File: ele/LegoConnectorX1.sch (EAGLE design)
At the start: 2 parts, among them X1 NXT-SOCKET

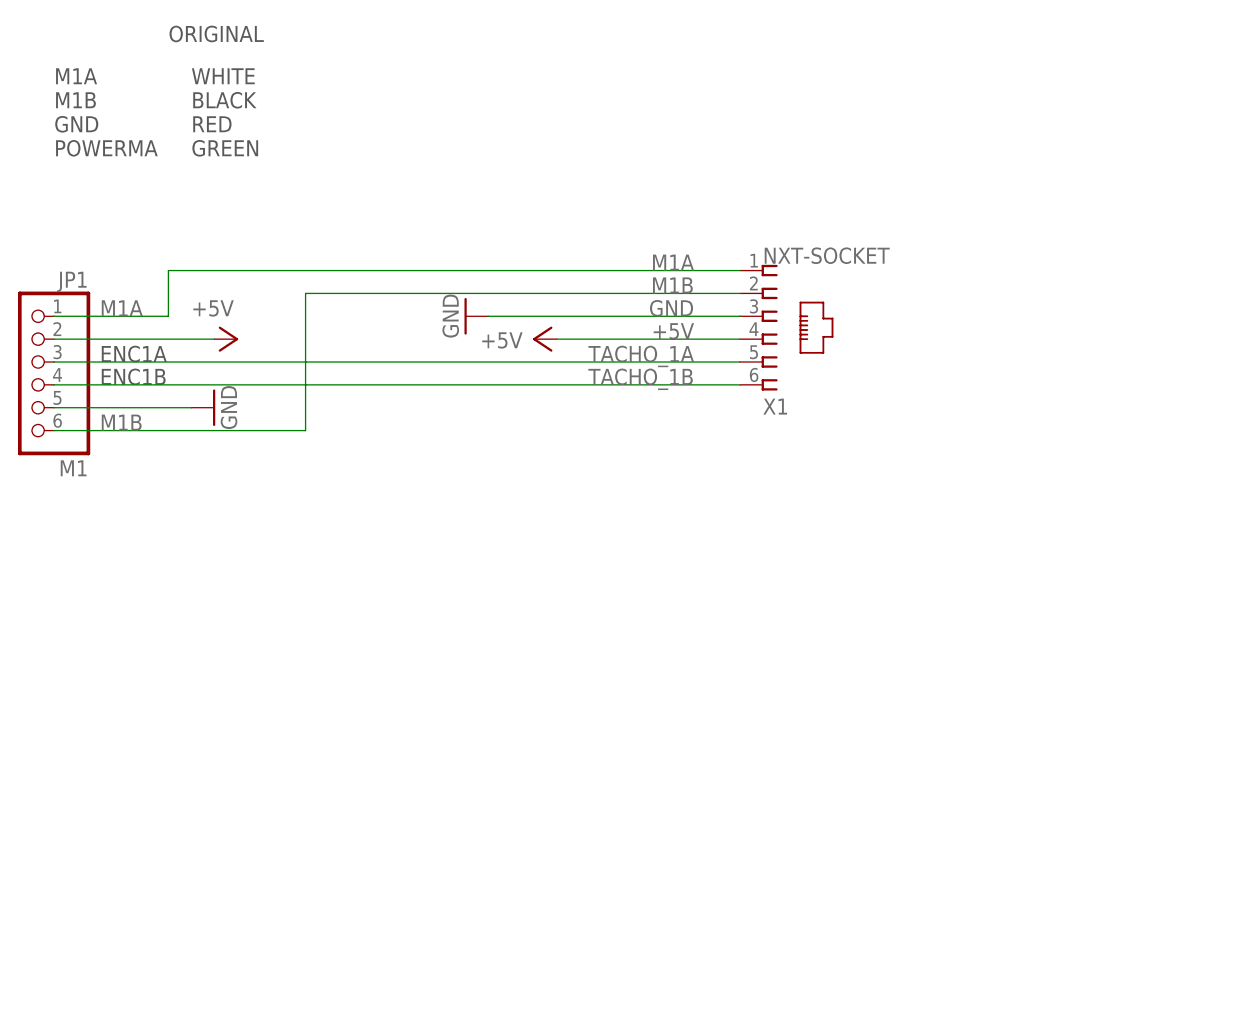
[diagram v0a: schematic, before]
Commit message: Add licenses to Eagle files
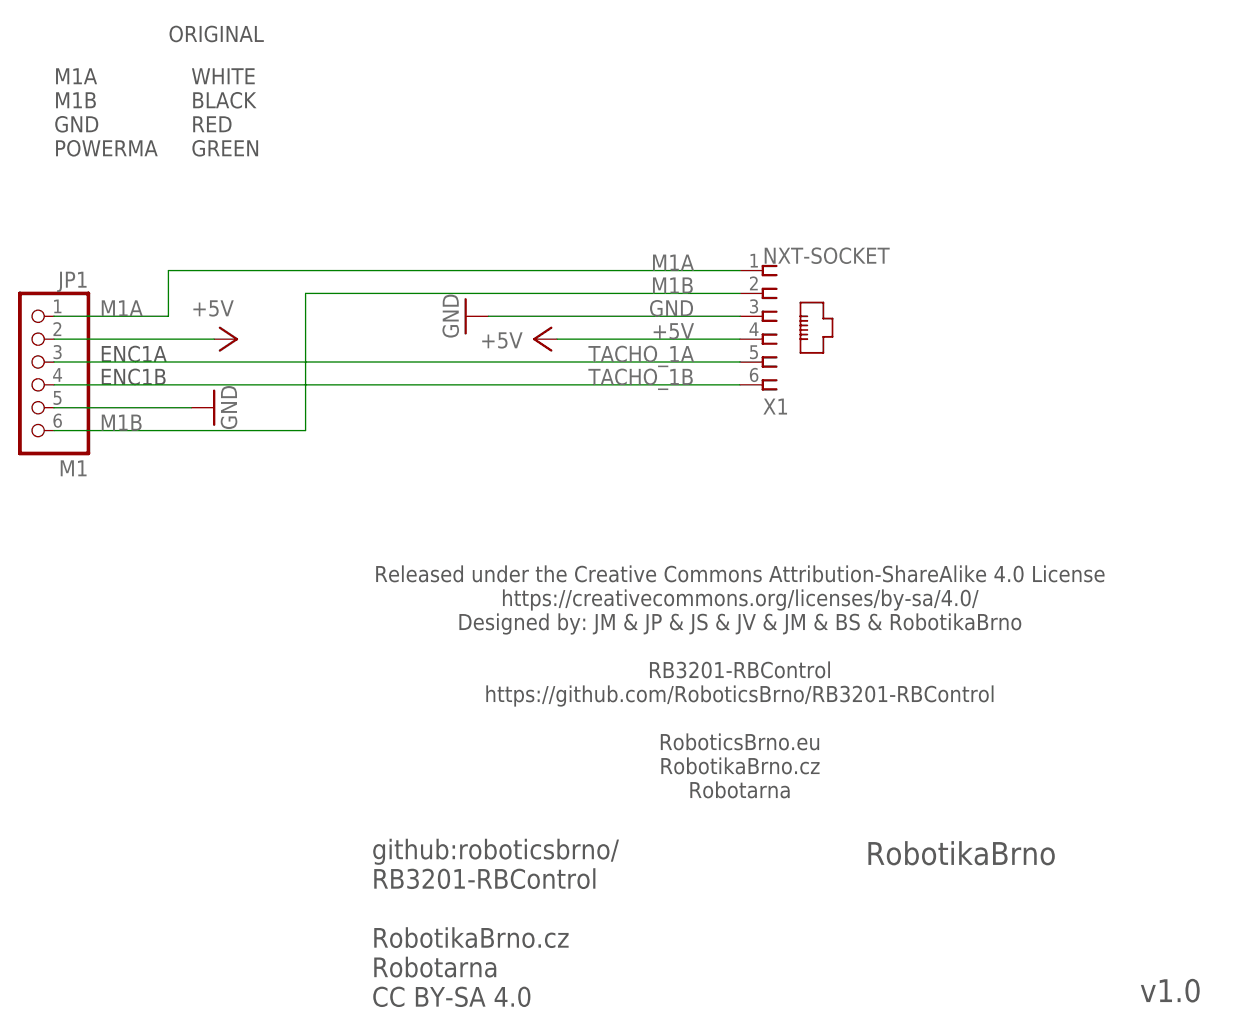
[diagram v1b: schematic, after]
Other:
- note added: "Released under the Creative Commons Attribution-ShareAlike 4.0 License https://creativecommons.org/licenses/by-sa/4.0/ Designed by: JM & JP & JS & JV & JM & BS & RobotikaBrno RB3201-RBControl https://github.com/RoboticsBrno/RB3201-RBControl RoboticsBrno.eu RobotikaBrno.cz Robotarna"
- note added: "RobotikaBrno"
- note added: "github:roboticsbrno/ RB3201-RBControl RobotikaBrno.cz Robotarna CC BY-SA 4.0"
- note added: "v1.0"
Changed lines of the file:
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@@
 <text x="55.88" y="73.66" size="1.778" layer="97">ENC1B</text>
 <text x="55.88" y="76.2" size="1.778" layer="97">ENC1A</text>
+<text x="86.106" y="4.572" size="2.1844" layer="97" font="vector">github:roboticsbrno/
+RB3201-RBControl
+RobotikaBrno.cz
+Robotarna
+CC BY-SA 4.0</text>
+<text x="140.97" y="20.32" size="2.54" layer="97" font="vector" ratio="14">RobotikaBrno</text>
+<text x="171.45" y="5.08" size="2.54" layer="97" font="vector" ratio="14">v1.0</text>
+<text x="127" y="40.64" size="1.778" layer="97" font="vector" align="center">Released under the Creative Commons Attribution-ShareAlike 4.0 License
+https://creativecommons.org/licenses/by-sa/4.0/
+Designed by: JM &amp; JP &amp; JS &amp; JV &amp; JM &amp; BS &amp; RobotikaBrno
+RB3201-RBControl
+https://github.com/RoboticsBrno/RB3201-RBControl
+RoboticsBrno.eu
+RobotikaBrno.cz
+Robotarna</text>
 </plain>
 <instances>
